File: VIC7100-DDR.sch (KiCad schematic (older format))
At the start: 13 parts, among them U13 VIC7100

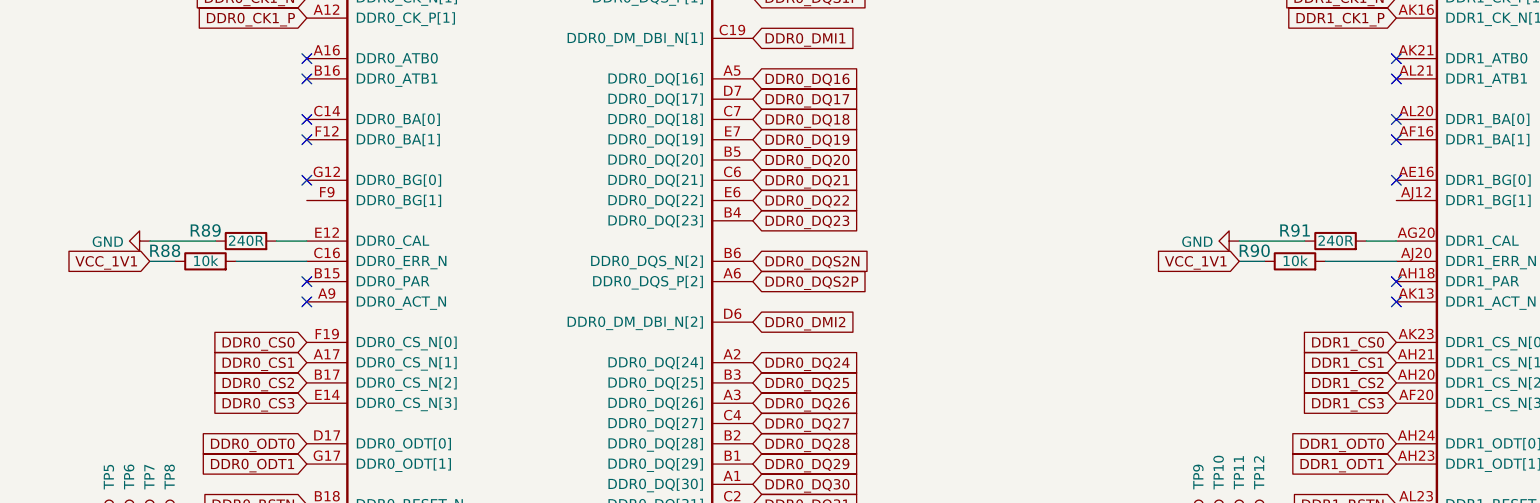
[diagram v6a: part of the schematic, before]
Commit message: Updated GPIO pinout to BV0.9. Remapped DSI. Mapped USB3.0
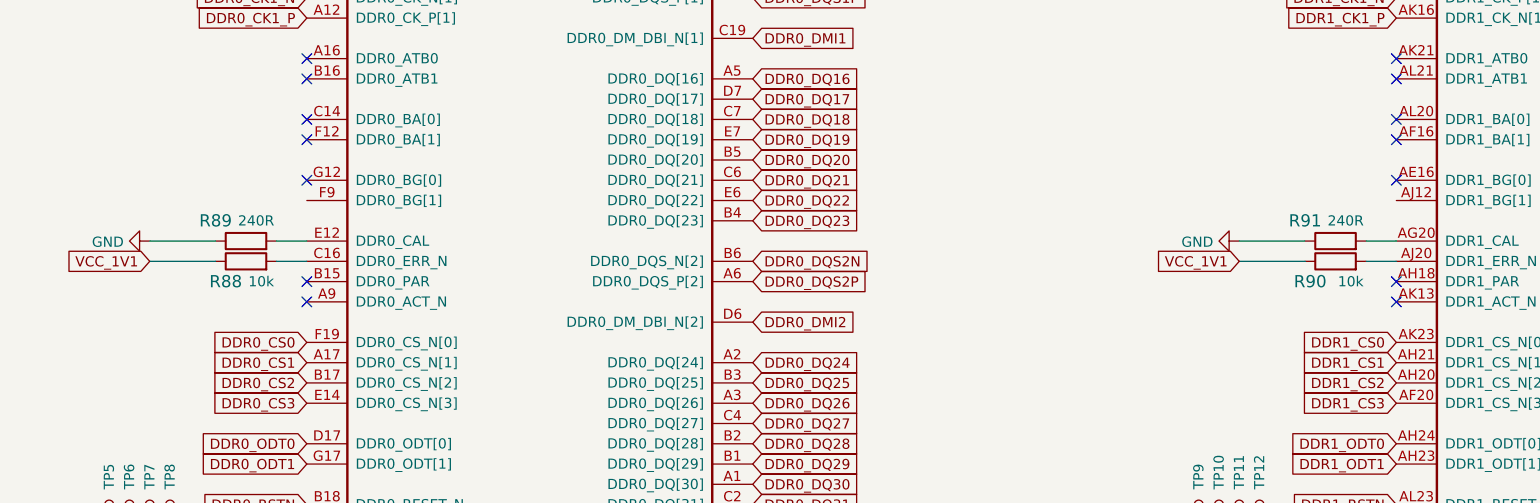
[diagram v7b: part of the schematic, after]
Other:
- moved on the sheet: R88, R90
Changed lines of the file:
@@
 U 1 1 615EA23C
 P 3900 5850
-F 0 "R89" H 3700 5900 60  0000 C CNN
+F 0 "R89" H 3750 5950 60  0000 C CNN
 F 1 "R_240R_0402" H 3900 5700 60  0001 C CNN
 F 2 "arvsom-footprints:0402-res" H 4100 6050 60  0001 L CNN
@@
 F 4 "PANASONIC" H 4100 6250 60  0001 L CNN "Manufacturer"
 F 5 "ERJ2GEJ241X" H 4100 6150 60  0001 L CNN "MPN"
-F 6 "240R" H 3900 5850 50  0000 C CNN "Val"
+F 6 "240R" H 3950 5950 50  0000 C CNN "Val"
 	1    3900 5850
 	1    0    0    -1
@@
 L arvsom:R_10k_0402 R88
 U 1 1 615F0DBD
-P 3700 5950
-F 0 "R88" H 3500 6000 60  0000 C CNN
-F 1 "R_10k_0402" H 3700 5800 60  0001 C CNN
-F 2 "arvsom-footprints:0402-res" H 3900 6150 60  0001 L CNN
-F 3 "" H 3700 5950 50  0001 C CNN
-F 4 "VISHAY" H 3900 6350 60  0001 L CNN "Manufacturer"
-F 5 "CRCW040210K0FKEDHP" H 3900 6250 60  0001 L CNN "MPN"
-F 6 "10k" H 3700 5950 50  0000 C CNN "Val"
-	1    3700 5950
+P 3900 5950
+F 0 "R88" H 3800 5850 60  0000 C CNN
+F 1 "R_10k_0402" H 3900 5800 60  0001 C CNN
+F 2 "arvsom-footprints:0402-res" H 4100 6150 60  0001 L CNN
+F 3 "" H 3900 5950 50  0001 C CNN
+F 4 "VISHAY" H 4100 6350 60  0001 L CNN "Manufacturer"
+F 5 "CRCW040210K0FKEDHP" H 4100 6250 60  0001 L CNN "MPN"
+F 6 "10k" H 3975 5850 50  0000 C CNN "Val"
+	1    3900 5950
 	1    0    0    -1
 $EndComp
 Wire Wire Line
-	3850 5950 4200 5950
+	4050 5950 4200 5950
 Wire Wire Line
 	3750 5850 3425 5850
 Wire Wire Line
-	3550 5950 3425 5950
+	3750 5950 3425 5950
 $Comp
 L arvsom:GND #PWR0222
@@
 U 1 1 6170D5ED
 P 9275 5850
-F 0 "R91" H 9075 5900 60  0000 C CNN
+F 0 "R91" H 9125 5950 60  0000 C CNN
 F 1 "R_240R_0402" H 9275 5700 60  0001 C CNN
 F 2 "arvsom-footprints:0402-res" H 9475 6050 60  0001 L CNN
@@
 F 4 "PANASONIC" H 9475 6250 60  0001 L CNN "Manufacturer"
 F 5 "ERJ2GEJ241X" H 9475 6150 60  0001 L CNN "MPN"
-F 6 "240R" H 9275 5850 50  0000 C CNN "Val"
+F 6 "240R" H 9325 5950 50  0000 C CNN "Val"
 	1    9275 5850
 	1    0    0    -1
@@
 L arvsom:R_10k_0402 R90
 U 1 1 6170D5F7
-P 9075 5950
-F 0 "R90" H 8875 6000 60  0000 C CNN
-F 1 "R_10k_0402" H 9075 5800 60  0001 C CNN
-F 2 "arvsom-footprints:0402-res" H 9275 6150 60  0001 L CNN
-F 3 "" H 9075 5950 50  0001 C CNN
-F 4 "VISHAY" H 9275 6350 60  0001 L CNN "Manufacturer"
-F 5 "CRCW040210K0FKEDHP" H 9275 6250 60  0001 L CNN "MPN"
-F 6 "10k" H 9075 5950 50  0000 C CNN "Val"
-	1    9075 5950
+P 9275 5950
+F 0 "R90" H 9150 5850 60  0000 C CNN
+F 1 "R_10k_0402" H 9275 5800 60  0001 C CNN
+F 2 "arvsom-footprints:0402-res" H 9475 6150 60  0001 L CNN
+F 3 "" H 9275 5950 50  0001 C CNN
+F 4 "VISHAY" H 9475 6350 60  0001 L CNN "Manufacturer"
+F 5 "CRCW040210K0FKEDHP" H 9475 6250 60  0001 L CNN "MPN"
+F 6 "10k" H 9350 5850 50  0000 C CNN "Val"
+	1    9275 5950
 	1    0    0    -1
 $EndComp
 Wire Wire Line
-	9225 5950 9575 5950
+	9425 5950 9575 5950
 Wire Wire Line
 	9125 5850 8800 5850
 Wire Wire Line
-	8925 5950 8800 5950
+	9125 5950 8800 5950
 $Comp
 L arvsom:GND #PWR0223

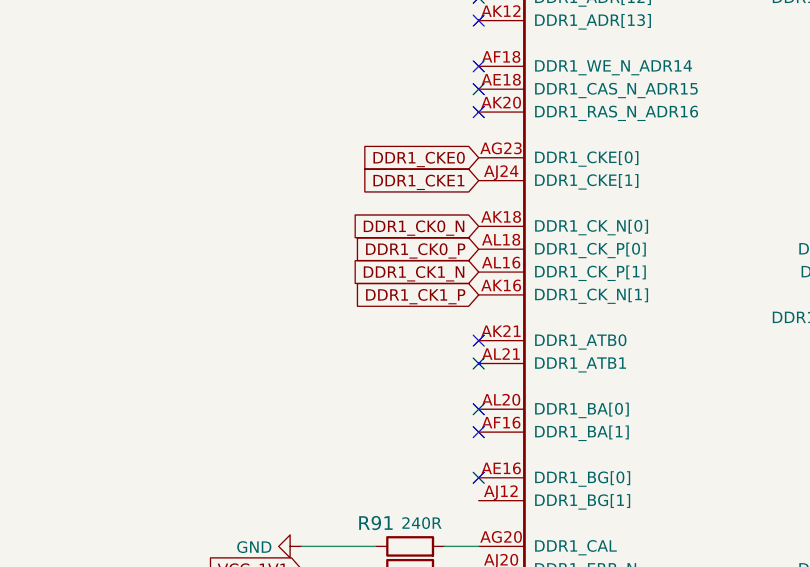
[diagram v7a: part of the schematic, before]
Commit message: Fixed two DDR pinout errors
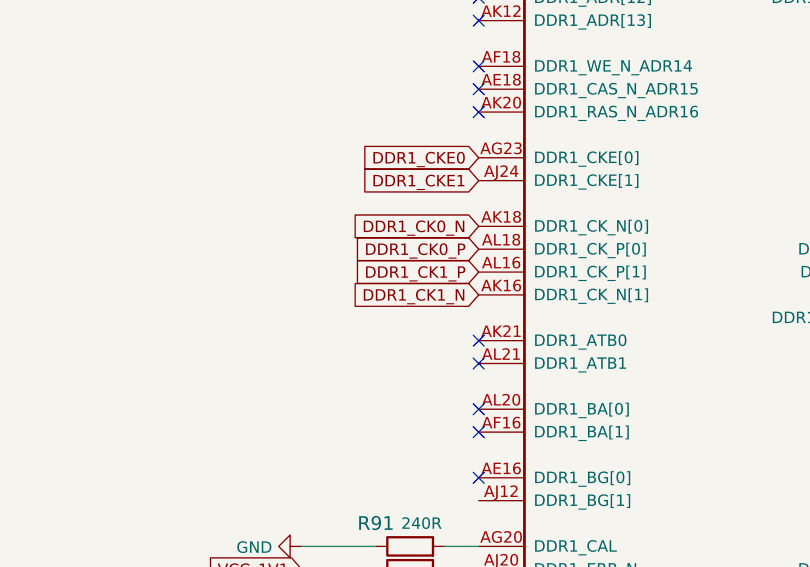
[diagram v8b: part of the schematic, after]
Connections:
- net DDR1_CK1_N: now also U13.AK16 (DDR1_CK_N[1]); no longer U13.AL16 (DDR1_CK_P[1])
- net DDR1_CK1_P: now also U13.AL16 (DDR1_CK_P[1]); no longer U13.AK16 (DDR1_CK_N[1])
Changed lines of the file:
@@
 Text GLabel 4200 4550 0    50   Input ~ 0
 DDR0_CK0_P
-Text GLabel 4200 4650 0    50   Input ~ 0
-DDR0_CK1_N
-Text GLabel 4200 4750 0    50   Input ~ 0
-DDR0_CK1_P
 Text GLabel 4200 4150 0    50   Input ~ 0
 DDR0_CKE0
@@
 Text GLabel 9575 4550 0    50   Input ~ 0
 DDR1_CK0_P
-Text GLabel 9575 4650 0    50   Input ~ 0
-DDR1_CK1_N
 Text GLabel 9575 4750 0    50   Input ~ 0
+DDR1_CK1_N
+Text GLabel 9575 4650 0    50   Input ~ 0
 DDR1_CK1_P
 Text GLabel 9575 4150 0    50   Input ~ 0
@@
 Text Notes 7550 1375 0    118  ~ 24
 VIC7100 DDR
+Text GLabel 4200 4750 0    50   Input ~ 0
+DDR0_CK1_P
+Text GLabel 4200 4650 0    50   Input ~ 0
+DDR0_CK1_N
 $EndSCHEMATC
